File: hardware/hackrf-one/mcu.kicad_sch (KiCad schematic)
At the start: 134 parts

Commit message: HackRF One: update trace widths for new stack-up
correct or ignore ERC/DRC errors
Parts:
- C118, C157, C158, C164: value (none) -> 18pF; footprint (none) -> hackrf:GSG-0402
- C125: value (none) -> 33pF; footprint (none) -> hackrf:GSG-0402
- C126, C127, C143, C145, C146: value (none) -> 10uF; footprint (none) -> hackrf:GSG-0805
- C128, C129, C130, C131, C132, C133, C134, C135, C136, C137, C138, C139, C140, C141, C142, C144, C147, C148, C149, C150, C151, C152, C153, C154: value (none) -> 100nF; footprint (none) -> hackrf:GSG-0402
- C155, R35: value (none) -> DNP; footprint (none) -> hackrf:GSG-0805
- C156: value (none) -> 47pF; footprint (none) -> hackrf:GSG-0402
- D2: value (none) -> VAALED; footprint (none) -> gsg-modules:LTST-S220
- D4: value (none) -> USBLED; footprint (none) -> gsg-modules:LTST-S220
- D5: value (none) -> RXLED; footprint (none) -> gsg-modules:LTST-S220
- D6: value (none) -> TXLED; footprint (none) -> gsg-modules:LTST-S220
- D7: value (none) -> VCCLED; footprint (none) -> gsg-modules:LTST-S220
- D8: value (none) -> 1V8LED; footprint (none) -> gsg-modules:LTST-S220
- FB3: value (none) -> FILTER; footprint (none) -> hackrf:GSG-0805
- J1: value (none) -> USB-MICRO-B; footprint (none) -> hackrf:GSG-USB-MICROB-FCI-10103592-EXT
- L10, L11: value (none) -> 4u7; footprint (none) -> hackrf:GSG-NRG4026
- NT1: value (none) -> 1V8; footprint (none) -> gsg-modules:HEADER-1x2-SHORTED
- NT2: value (none) -> VCC; footprint (none) -> gsg-modules:HEADER-1x2-SHORTED
- P20: value (none) -> GPIO; footprint (none) -> hackrf:GSG-HEADER-2x11
- P22: value (none) -> I2S; footprint (none) -> hackrf:GSG-HEADER-2x13
- P23: value (none) -> DBGEN; footprint (none) -> hackrf:GSG-TESTPOINT-50MIL
- P24: value (none) -> TRST; footprint (none) -> hackrf:GSG-TESTPOINT-50MIL
- P25: value (none) -> LPC_ISP; footprint (none) -> hackrf:GSG-HEADER-1x6
- P26: value (none) -> LPC_JTAG; footprint (none) -> hackrf:GSG-50MIL-HEADER-2x5-TH
- P28: value (none) -> SD; footprint (none) -> hackrf:GSG-HEADER-2x11
- P29: value (none) -> CPLD_JTAG; footprint (none) -> hackrf:GSG-HEADER-1x2
- P3: value (none) -> GND; footprint (none) -> hackrf:GSG-HEADER-NOMARK-1x2
- P30: value (none) -> BANK2_AUX; footprint (none) -> hackrf:GSG-HEADER-2x10
- P5: value (none) -> LEDS; footprint (none) -> hackrf:GSG-HEADER-2x3
- P68: value (none) -> SPIFI_CS; footprint (none) -> hackrf:GSG-TESTPOINT-50MIL
- P69: value (none) -> VREGMODE; footprint (none) -> hackrf:GSG-TESTPOINT-50MIL
- P70: value (none) -> EN_1V8; footprint (none) -> hackrf:GSG-TESTPOINT-50MIL
- P71: value (none) -> ID; footprint (none) -> hackrf:GSG-TESTPOINT-50MIL
- P72, P75, P76, P77, P78, P79: value (none) -> GP_CLKIN; footprint (none) -> hackrf:GSG-TESTPOINT-50MIL
- P73: value (none) -> P1_2; footprint (none) -> hackrf:GSG-TESTPOINT-50MIL
- P74: value (none) -> P1_1; footprint (none) -> hackrf:GSG-TESTPOINT-50MIL
- P80: value (none) -> SHIELD; footprint (none) -> hackrf:GSG-HEADER-NOMARK-1x2
- P81: value (none) -> SPIFI_SIO2; footprint (none) -> hackrf:GSG-TESTPOINT-50MIL
- P82: value (none) -> SPIFI_SIO3; footprint (none) -> hackrf:GSG-TESTPOINT-50MIL
- Q5: value (none) -> MOSFET_P; footprint (none) -> gsg-modules:SOT23-3
- R100, R19, R30, R34, R77, R78, R79, R80, R81, R86, R87, R88, R89, R90, R91, R96, R98, R99: value (none) -> 39; footprint (none) -> hackrf:GSG-0402
- R12, R37, R48, R49, R51, R52, R54, R59, R62, R63, R64, R66, R67, R68, R7, R93: value (none) -> 10k; footprint (none) -> hackrf:GSG-0402
- R18, R74: value (none) -> 1k8; footprint (none) -> hackrf:GSG-0402
- R46, R55: value (none) -> 162k; footprint (none) -> hackrf:GSG-0402
- R47: value (none) -> 330k; footprint (none) -> hackrf:GSG-0402
- R56: value (none) -> 715k; footprint (none) -> hackrf:GSG-0402
- R57, R58: value (none) -> 0; footprint (none) -> hackrf:GSG-0402
- R65: value (none) -> 18k; footprint (none) -> hackrf:GSG-0402
- R69: value (none) -> 12k; footprint (none) -> hackrf:GSG-0402
- R72, R75: value (none) -> 470; footprint (none) -> hackrf:GSG-0402
- R73, R76: value (none) -> 1k; footprint (none) -> hackrf:GSG-0402
- SW1: value (none) -> DFU; footprint (none) -> hackrf:GSG-SWITCH-FSMRA
- SW2: value (none) -> RESET; footprint (none) -> hackrf:GSG-SWITCH-FSMRA
- U15: value (none) -> TVS; footprint (none) -> hackrf:GSG-LXES1TBCC2-004
- U20: value (none) -> W25Q80; footprint (none) -> hackrf:GSG-SOIC8-208
- U21: value (none) -> TPS62410; footprint (none) -> hackrf:GSG-S-PVSON-N10
- U23: value (none) -> LPC4320FBD144; footprint (none) -> hackrf:GSG-LQFP144
- U24: value (none) -> GSG-XC2C64A-7VQG100C; footprint (none) -> hackrf:GSG-VQ100
- X2: value (none) -> MCU_XTAL; footprint (none) -> hackrf:GSG-XTAL3.2x2.5mm
- X3: value (none) -> RTC_XTAL; footprint (none) -> hackrf:GSG-XTAL-AB26TRQ

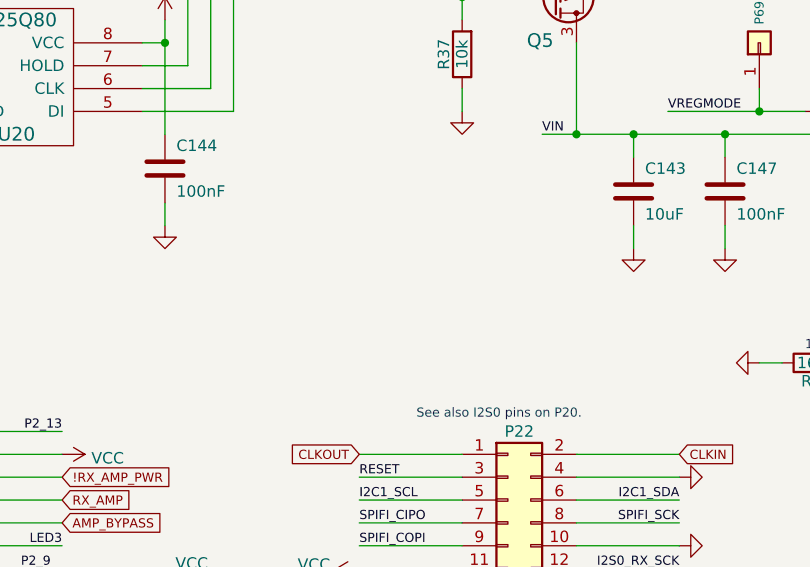
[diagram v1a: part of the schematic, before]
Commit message: HackRF One: correct or ignore ERC errors
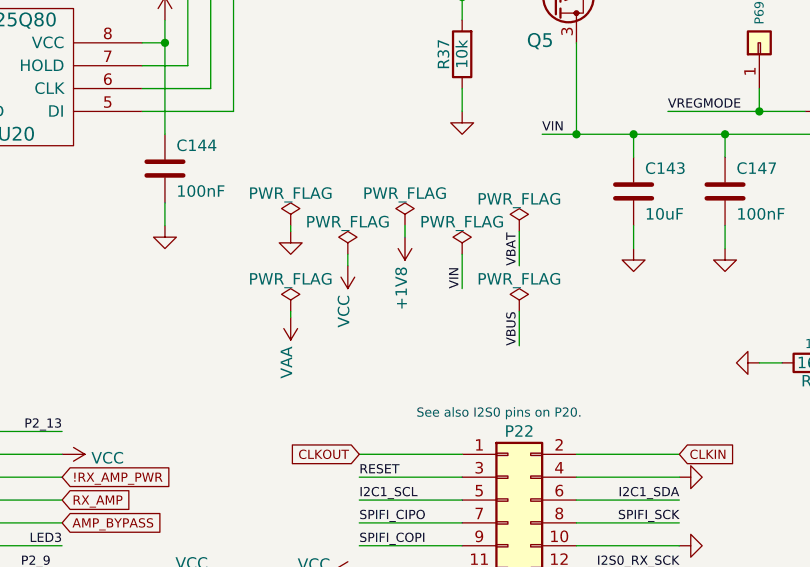
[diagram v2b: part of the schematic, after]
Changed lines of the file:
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@@
     (stroke (width 0) (type default) (color 0 0 0 0))
   )
+  (wire (pts (xy 279.4 62.865) (xy 279.4 63.5))
+    (stroke (width 0) (type default) (color 0 0 0 0))
+  )
   (wire (pts (xy 267.97 95.25) (xy 267.97 96.52))
     (stroke (width 0) (type default) (color 0 0 0 0))
@@
     (stroke (width 0) (type default) (color 0 0 0 0))
   )
+  (wire (pts (xy 292.1 53.34) (xy 292.1 54.61))
+    (stroke (width 0) (type default) (color 0 0 0 0))
+  )
   (wire (pts (xy 82.55 27.94) (xy 90.17 27.94))
     (stroke (width 0) (type default) (color 0 0 0 0))
@@
     (stroke (width 0) (type default) (color 0 0 0 0))
   )
+  (wire (pts (xy 304.8 57.785) (xy 304.8 53.975))
+    (stroke (width 0) (type default) (color 0 0 0 0))
+  )
   (wire (pts (xy 36.83 20.32) (xy 44.45 20.32))
     (stroke (width 0) (type default) (color 0 0 0 0))
@@
     (stroke (width 0) (type default) (color 0 0 0 0))
   )
+  (wire (pts (xy 285.75 56.515) (xy 285.75 57.785))
+    (stroke (width 0) (type default) (color 0 0 0 0))
+  )
   (wire (pts (xy 186.69 24.13) (xy 186.69 52.07))
     (stroke (width 0) (type default) (color 0 0 0 0))
@@
     (stroke (width 0) (type default) (color 0 0 0 0))
   )
+  (wire (pts (xy 304.8 66.675) (xy 304.8 62.865))
+    (stroke (width 0) (type default) (color 0 0 0 0))
+  )
   (wire (pts (xy 410.21 40.64) (xy 410.21 43.18))
     (stroke (width 0) (type default) (color 0 0 0 0))
@@
     (stroke (width 0) (type default) (color 0 0 0 0))
   )
+  (wire (pts (xy 279.4 53.34) (xy 279.4 53.975))
+    (stroke (width 0) (type default) (color 0 0 0 0))
+  )
   (wire (pts (xy 33.02 46.99) (xy 33.02 57.15))
     (stroke (width 0) (type default) (color 0 0 0 0))
@@
     (stroke (width 0) (type default) (color 0 0 0 0))
   )
+  (wire (pts (xy 298.45 60.325) (xy 298.45 56.515))
+    (stroke (width 0) (type default) (color 0 0 0 0))
+  )
   (wire (pts (xy 106.68 245.11) (xy 109.22 245.11))
     (stroke (width 0) (type default) (color 0 0 0 0))
@@
     (effects (font (size 1.016 1.016)) (justify left bottom))
   )
+  (label "VBUS" (at 304.8 66.675 90)
+    (effects (font (size 1.016 1.016)) (justify left bottom))
+  )
   (label "LED3" (at 33.02 157.48 270)
     (effects (font (size 1.016 1.016)) (justify right bottom))
@@
     (effects (font (size 1.016 1.016)) (justify left bottom))
   )
+  (label "VIN" (at 298.45 60.325 90)
+    (effects (font (size 1.016 1.016)) (justify left bottom))
+  )
   (label "CPLD_TMS" (at 368.3 234.95 90)
     (effects (font (size 1.016 1.016)) (justify left bottom))
@@
     (effects (font (size 1.016 1.016)) (justify left bottom))
   )
+  (label "VBAT" (at 304.8 57.785 90)
+    (effects (font (size 1.016 1.016)) (justify left bottom))
+  )
   (label "SGPIO0" (at 101.6 154.94 0)
     (effects (font (size 1.016 1.016)) (justify left bottom))
@@
       (effects (font (size 1.27 1.27)) hide)
     )
+    (pin "1")
+  )
+  (symbol (lib_id "power:PWR_FLAG") (at 304.8 62.865 0) (unit 1)
+    (in_bom yes) (on_board yes) (fields_autoplaced)
+    (property "Reference" "#FLG0106" (id 0) (at 304.8 60.96 0)
+      (effects (font (size 1.27 1.27)) hide)
+    )
+    (property "Value" "PWR_FLAG" (id 1) (at 304.8 59.2892 0))
+    (property "Footprint" "" (id 2) (at 304.8 62.865 0)
+      (effects (font (size 1.27 1.27)) hide)
+    )
+    (property "Datasheet" "~" (id 3) (at 304.8 62.865 0)
+      (effects (font (size 1.27 1.27)) hide)
+    )
+    (pin "1")
+  )
+  (symbol (lib_id "power:PWR_FLAG") (at 279.4 53.34 0) (unit 1)
+    (in_bom yes) (on_board yes) (fields_autoplaced)
+    (property "Reference" "#FLG0101" (id 0) (at 279.4 51.435 0)
+      (effects (font (size 1.27 1.27)) hide)
+    )
+    (property "Value" "PWR_FLAG" (id 1) (at 279.4 49.7642 0))
+    (property "Footprint" "" (id 2) (at 279.4 53.34 0)
+      (effects (font (size 1.27 1.27)) hide)
+    )
+    (property "Datasheet" "~" (id 3) (at 279.4 53.34 0)
+      (effects (font (size 1.27 1.27)) hide)
+    )
+    (pin "1")
+  )
+  (symbol (lib_id "power:PWR_FLAG") (at 304.8 53.975 0) (unit 1)
+    (in_bom yes) (on_board yes) (fields_autoplaced)
+    (property "Reference" "#FLG01" (id 0) (at 304.8 52.07 0)
+      (effects (font (size 1.27 1.27)) hide)
+    )
+    (property "Value" "PWR_FLAG" (id 1) (at 304.8 50.3992 0))
+    (property "Footprint" "" (id 2) (at 304.8 53.975 0)
+      (effects (font (size 1.27 1.27)) hide)
+    )
+    (property "Datasheet" "~" (id 3) (at 304.8 53.975 0)
+      (effects (font (size 1.27 1.27)) hide)
+    )
+    (pin "1")
+  )
+  (symbol (lib_id "power:PWR_FLAG") (at 292.1 53.34 0) (unit 1)
+    (in_bom yes) (on_board yes) (fields_autoplaced)
+    (property "Reference" "#FLG0102" (id 0) (at 292.1 51.435 0)
+      (effects (font (size 1.27 1.27)) hide)
+    )
+    (property "Value" "PWR_FLAG" (id 1) (at 292.1 49.7642 0))
+    (property "Footprint" "" (id 2) (at 292.1 53.34 0)
+      (effects (font (size 1.27 1.27)) hide)
+    )
+    (property "Datasheet" "~" (id 3) (at 292.1 53.34 0)
+      (effects (font (size 1.27 1.27)) hide)
+    )
+    (pin "1")
+  )
+  (symbol (lib_id "power:PWR_FLAG") (at 285.75 56.515 0) (unit 1)
+    (in_bom yes) (on_board yes) (fields_autoplaced)
+    (property "Reference" "#FLG0104" (id 0) (at 285.75 54.61 0)
+      (effects (font (size 1.27 1.27)) hide)
+    )
+    (property "Value" "PWR_FLAG" (id 1) (at 285.75 52.9392 0))
+    (property "Footprint" "" (id 2) (at 285.75 56.515 0)
+      (effects (font (size 1.27 1.27)) hide)
+    )
+    (property "Datasheet" "~" (id 3) (at 285.75 56.515 0)
+      (effects (font (size 1.27 1.27)) hide)
+    )
+    (pin "1")
+  )
+  (symbol (lib_id "power:VAA") (at 279.4 63.5 180) (unit 1)
+    (in_bom yes) (on_board yes)
+    (property "Reference" "#PWR0333" (id 0) (at 279.4 59.69 0)
+      (effects (font (size 1.27 1.27)) hide)
+    )
+    (property "Value" "VAA" (id 1) (at 278.9682 66.7512 90)
+      (effects (font (size 1.27 1.27)) (justify left))
+    )
+    (property "Footprint" "" (id 2) (at 279.4 63.5 0)
+      (effects (font (size 1.27 1.27)) hide)
+    )
+    (property "Datasheet" "" (id 3) (at 279.4 63.5 0)
+      (effects (font (size 1.27 1.27)) hide)
+    )
+    (pin "1")
+  )
+  (symbol (lib_id "power:PWR_FLAG") (at 298.45 56.515 0) (unit 1)
+    (in_bom yes) (on_board yes) (fields_autoplaced)
+    (property "Reference" "#FLG0103" (id 0) (at 298.45 54.61 0)
+      (effects (font (size 1.27 1.27)) hide)
+    )
+    (property "Value" "PWR_FLAG" (id 1) (at 298.45 52.9392 0))
+    (property "Footprint" "" (id 2) (at 298.45 56.515 0)
+      (effects (font (size 1.27 1.27)) hide)
+    )
+    (property "Datasheet" "~" (id 3) (at 298.45 56.515 0)
+      (effects (font (size 1.27 1.27)) hide)
+    )
+    (pin "1")
+  )
+  (symbol (lib_id "power:+1V8") (at 292.1 54.61 180) (unit 1)
+    (in_bom yes) (on_board yes)
+    (property "Reference" "#PWR0332" (id 0) (at 292.1 50.8 0)
+      (effects (font (size 1.27 1.27)) hide)
+    )
+    (property "Value" "+1V8" (id 1) (at 291.719 57.8612 90)
+      (effects (font (size 1.27 1.27)) (justify left))
+    )
+    (property "Footprint" "" (id 2) (at 292.1 54.61 0)
+      (effects (font (size 1.27 1.27)) hide)
+    )
+    (property "Datasheet" "" (id 3) (at 292.1 54.61 0)
+      (effects (font (size 1.27 1.27)) hide)
+    )
+    (pin "1")
+  )
+  (symbol (lib_id "power:GND") (at 279.4 53.975 0) (unit 1)
+    (in_bom yes) (on_board yes)
+    (property "Reference" "#PWR0330" (id 0) (at 279.4 53.975 0)
+      (effects (font (size 0.762 0.762)) hide)
+    )
+    (property "Value" "GND" (id 1) (at 279.4 55.753 0)
+      (effects (font (size 0.762 0.762)) hide)
+    )
+    (property "Footprint" "" (id 2) (at 279.4 53.975 0)
+      (effects (font (size 1.524 1.524)) hide)
+    )
+    (property "Datasheet" "" (id 3) (at 279.4 53.975 0)
+      (effects (font (size 1.524 1.524)) hide)
+    )
+    (pin "1")
+  )
+  (symbol (lib_id "power:PWR_FLAG") (at 279.4 62.865 0) (unit 1)
+    (in_bom yes) (on_board yes) (fields_autoplaced)
+    (property "Reference" "#FLG0105" (id 0) (at 279.4 60.96 0)
+      (effects (font (size 1.27 1.27)) hide)
+    )
+    (property "Value" "PWR_FLAG" (id 1) (at 279.4 59.2892 0))
+    (property "Footprint" "" (id 2) (at 279.4 62.865 0)
+      (effects (font (size 1.27 1.27)) hide)
+    )
+    (property "Datasheet" "~" (id 3) (at 279.4 62.865 0)
+      (effects (font (size 1.27 1.27)) hide)
+    )
+    (pin "1")
+  )
+  (symbol (lib_id "power:VCC") (at 285.75 57.785 180) (unit 1)
+    (in_bom yes) (on_board yes)
+    (property "Reference" "#PWR0331" (id 0) (at 285.75 53.975 0)
+      (effects (font (size 1.27 1.27)) hide)
+    )
+    (property "Value" "VCC" (id 1) (at 285.3182 61.0362 90)
+      (effects (font (size 1.27 1.27)) (justify left))
+    )
+    (property "Footprint" "" (id 2) (at 285.75 57.785 0)
+      (effects (font (size 1.27 1.27)) hide)
+    )
+    (property "Datasheet" "" (id 3) (at 285.75 57.785 0)
+      (effects (font (size 1.27 1.27)) hide)
+    )

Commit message: HackRF One: update dates
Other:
- company: Copyright 2012-2020 Great Scott Gadgets -> Copyright 2012-2022 Great Scott Gadgets
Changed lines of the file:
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@@
   (title_block
     (title "HackRF One")
-    (date "2021-09-28")
+    (date "2022-08-28")
     (rev "r9")
-    (company "Copyright 2012-2020 Great Scott Gadgets")
+    (company "Copyright 2012-2022 Great Scott Gadgets")
     (comment 1 "Michael Ossmann")
     (comment 2 "Licensed under the CERN-OHL-P v2")
